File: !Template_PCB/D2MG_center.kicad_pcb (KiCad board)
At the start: 2 copper layers, 33 x 58.5 mm, 0 parts

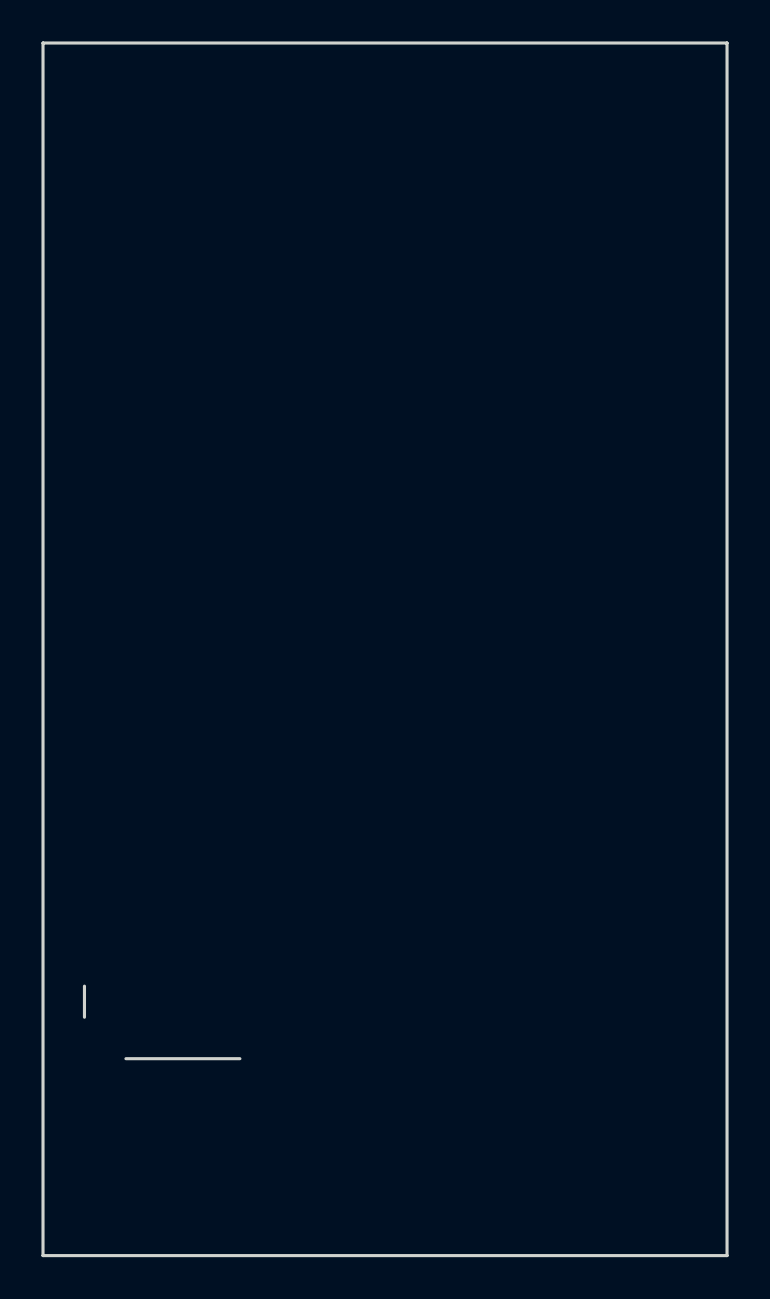
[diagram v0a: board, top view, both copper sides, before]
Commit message: + Spruce_60x70 Template_PCB
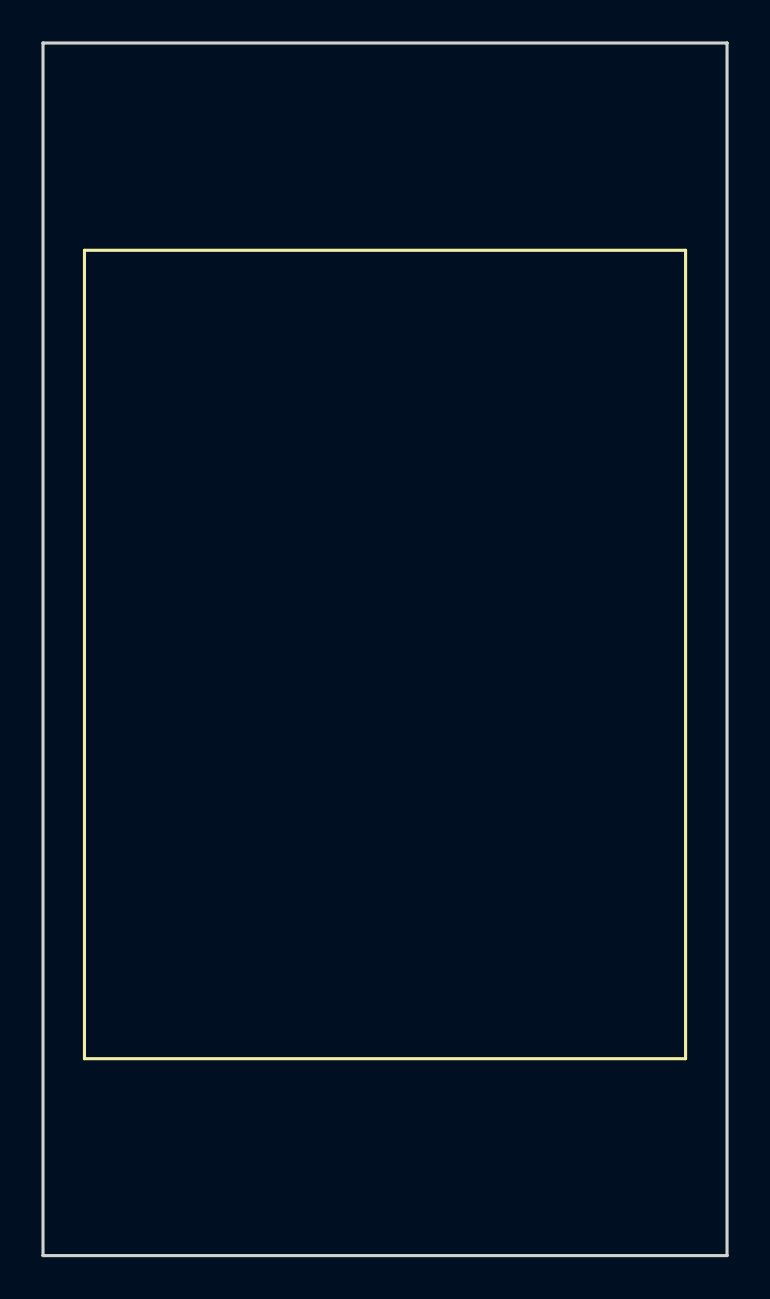
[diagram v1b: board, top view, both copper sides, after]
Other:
- outline, holes or cut-outs redrawn
- board text removed: "bottom"
- board text removed: "top"
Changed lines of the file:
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@@
     (area 97.924999 47.924999 135.075001 110.575001)
     (thickness 1.6)
-    (drawings 29)
+    (drawings 24)
     (tracks 0)
     (zones 0)
@@
     (uvia_drill 0.3)
   )
-  (gr_text top (at 104 98) (layer Dwgs.User)
-    (effects (font (size 1.5 1.5) (thickness 0.3)))
-  )
-  (gr_text bottom (at 116.5 52.5) (layer Dwgs.User)
-    (effects (font (size 1.5 1.5) (thickness 0.3)))
-  )
-  (gr_text bottom (at 116.5 106.5) (layer Dwgs.User)
-    (effects (font (size 1.5 1.5) (thickness 0.3)))
-  )
-  (gr_line (start 118.5 51) (end 118.5 50) (angle 90) (layer Dwgs.User) (width 0.15))
-  (gr_line (start 114.5 51) (end 118.5 51) (angle 90) (layer Dwgs.User) (width 0.15))
-  (gr_line (start 114.5 50) (end 114.5 51) (angle 90) (layer Dwgs.User) (width 0.15))
-  (gr_line (start 118.5 107.5) (end 118.5 108.5) (angle 90) (layer Dwgs.User) (width 0.15))
-  (gr_line (start 114.5 107.5) (end 118.5 107.5) (angle 90) (layer Dwgs.User) (width 0.15))
-  (gr_line (start 114.5 108.5) (end 114.5 107.5) (angle 90) (layer Dwgs.User) (width 0.15))
+  (gr_line (start 118.5 51) (end 118.5 50) (angle 90) (layer B.SilkS) (width 0.15))
+  (gr_line (start 114.5 51) (end 118.5 51) (angle 90) (layer B.SilkS) (width 0.15))
+  (gr_line (start 114.5 50) (end 114.5 51) (angle 90) (layer B.SilkS) (width 0.15))
+  (gr_line (start 118.5 107.5) (end 118.5 108.5) (angle 90) (layer B.SilkS) (width 0.15))
+  (gr_line (start 114.5 107.5) (end 118.5 107.5) (angle 90) (layer B.SilkS) (width 0.15))
+  (gr_line (start 114.5 108.5) (end 114.5 107.5) (angle 90) (layer B.SilkS) (width 0.15))
   (gr_line (start 116.5 107.5) (end 116.5 110.5) (angle 90) (layer Dwgs.User) (width 0.15))
   (gr_line (start 116.5 51) (end 116.5 48) (angle 90) (layer Dwgs.User) (width 0.15))
   (gr_line (start 133 108.5) (end 133 50) (angle 90) (layer Edge.Cuts) (width 0.15))
   (gr_line (start 100 108.5) (end 100 50) (angle 90) (layer Edge.Cuts) (width 0.15))
-  (gr_line (start 109.5 99) (end 104 99) (angle 90) (layer Edge.Cuts) (width 0.15))
-  (gr_line (start 102 97) (end 102 95.5) (angle 90) (layer Edge.Cuts) (width 0.15))
   (gr_line (start 117 79.5) (end 119 79.5) (angle 90) (layer Dwgs.User) (width 0.15))
   (gr_text 0x0 (at 118.25 79) (layer Dwgs.User)
@@
   (gr_line (start 101 79.5) (end 98 79.5) (angle 90) (layer Dwgs.User) (width 0.15))
   (gr_line (start 132 79.5) (end 135 79.5) (angle 90) (layer Dwgs.User) (width 0.15))
-  (gr_line (start 102 60) (end 131 60) (angle 90) (layer Dwgs.User) (width 0.15))
-  (gr_line (start 102 99) (end 102 60) (angle 90) (layer Dwgs.User) (width 0.15))
-  (gr_line (start 131 99) (end 102 99) (angle 90) (layer Dwgs.User) (width 0.15))
-  (gr_line (start 131 60) (end 131 99) (angle 90) (layer Dwgs.User) (width 0.15))
+  (gr_line (start 102 60) (end 131 60) (angle 90) (layer F.SilkS) (width 0.15))
+  (gr_line (start 102 99) (end 102 60) (angle 90) (layer F.SilkS) (width 0.15))
+  (gr_line (start 131 99) (end 102 99) (angle 90) (layer F.SilkS) (width 0.15))
+  (gr_line (start 131 60) (end 131 99) (angle 90) (layer F.SilkS) (width 0.15))
   (gr_line (start 133 108.5) (end 100 108.5) (angle 90) (layer Edge.Cuts) (width 0.15))
   (gr_line (start 100 50) (end 133 50) (angle 90) (layer Edge.Cuts) (width 0.15))
